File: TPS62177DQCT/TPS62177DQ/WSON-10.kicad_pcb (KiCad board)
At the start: 2 copper layers, 13.8 x 16.4 mm, 3 parts, among them J1 Conn_01x06_Male, J2 Conn_01x06_Male, U1 TPS62177DQC

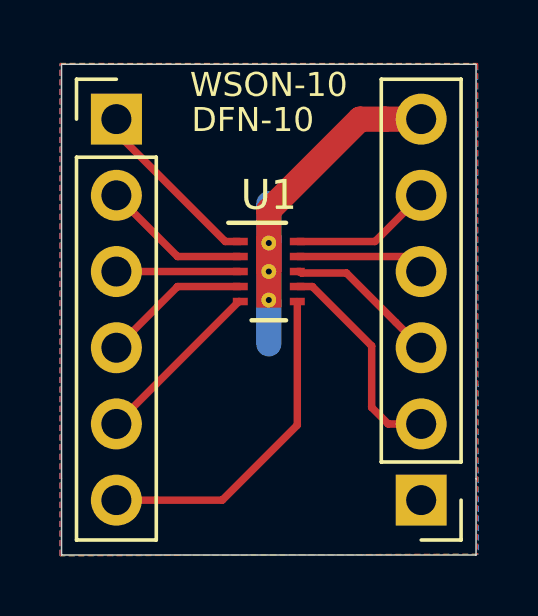
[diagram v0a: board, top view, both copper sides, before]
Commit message: Add gerbers for the TPS62 module
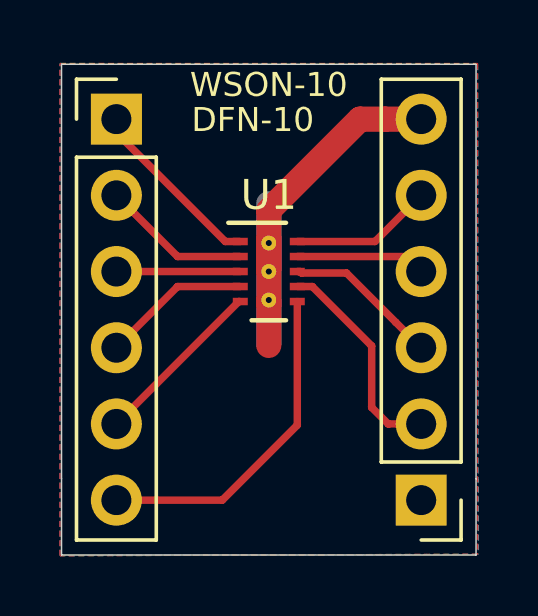
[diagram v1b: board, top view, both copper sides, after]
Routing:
- net PAD: track 11.2 -> 12.7 mm
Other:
- board text added: "Thermal relief between the top and bottom copper layers is specifically for the TPS62177DQ Buck Regulator. However this board could be used for other WSON-10 or small width DFN-10 type packages using a reflow soldering method."
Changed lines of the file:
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@@
   (general
     (thickness 1.6)
-    (drawings 8)
-    (tracks 33)
+    (drawings 9)
+    (tracks 34)
     (zones 0)
     (modules 3)
@@
   )
   (setup
-    (last_trace_width 0.84)
+    (last_trace_width 0.25)
     (user_trace_width 0.25)
     (user_trace_width 0.84)
@@
     )
   )
+  (gr_text "Thermal relief between the top and bottom copper layers is specifically \nfor the TPS62177DQ Buck Regulator. However this board could be used\nfor other WSON-10 or small width DFN-10 type packages using a reflow\nsoldering method. " (at 67.2846 72.6948) (layer Cmts.User)
+    (effects (font (size 1.5 1.5) (thickness 0.3)))
+  )
   (gr_line (start 74.0664 63.8048) (end 74.0664 66.3448) (layer Edge.Cuts) (width 0.05))
   (gr_line (start 60.2488 66.3448) (end 74.0664 66.3448) (layer Edge.Cuts) (width 0.05))
@@
   (segment (start 67.1576 56.896) (end 67.1576 54.856) (width 0.84) (layer F.Cu) (net 1))
   (segment (start 67.1576 54.856) (end 70.1976 51.816) (width 0.84) (layer F.Cu) (net 1))
+  (segment (start 67.1576 57.846) (end 67.1576 59.3598) (width 0.84) (layer F.Cu) (net 1))
   (segment (start 70.6976 55.896) (end 72.2376 54.356) (width 0.25) (layer F.Cu) (net 2))
   (segment (start 68.1076 55.896) (end 70.6976 55.896) (width 0.25) (layer F.Cu) (net 2))
